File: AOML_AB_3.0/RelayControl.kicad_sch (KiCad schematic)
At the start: 41 parts, among them IC1 CD4043BDR, IC2 CD4043BDR, J5 Conn_01x03, K1 TX2-L2-5V, K10 TX2-L2-5V, K11 TX2-L2-5V, K12 TX2-L2-5V, K13 TX2-L2-5V, K2 TX2-L2-5V, K3 TX2-L2-5V, K4 TX2-L2-5V, K5 TX2-L2-5V, K6 TX2-L2-5V, K7 TX2-L2-5V, K8 TX2-L2-5V, K9 TX2-L2-5V, U10 TLP170AM, U11 TLP170AM, U12 TLP170AM, U13 TLP170AM, U14 TLP170AM, U5 ULN2003, U6 ULN2003, U7 TLP170AM, U8 TLP170AM, U9 TLP170AM

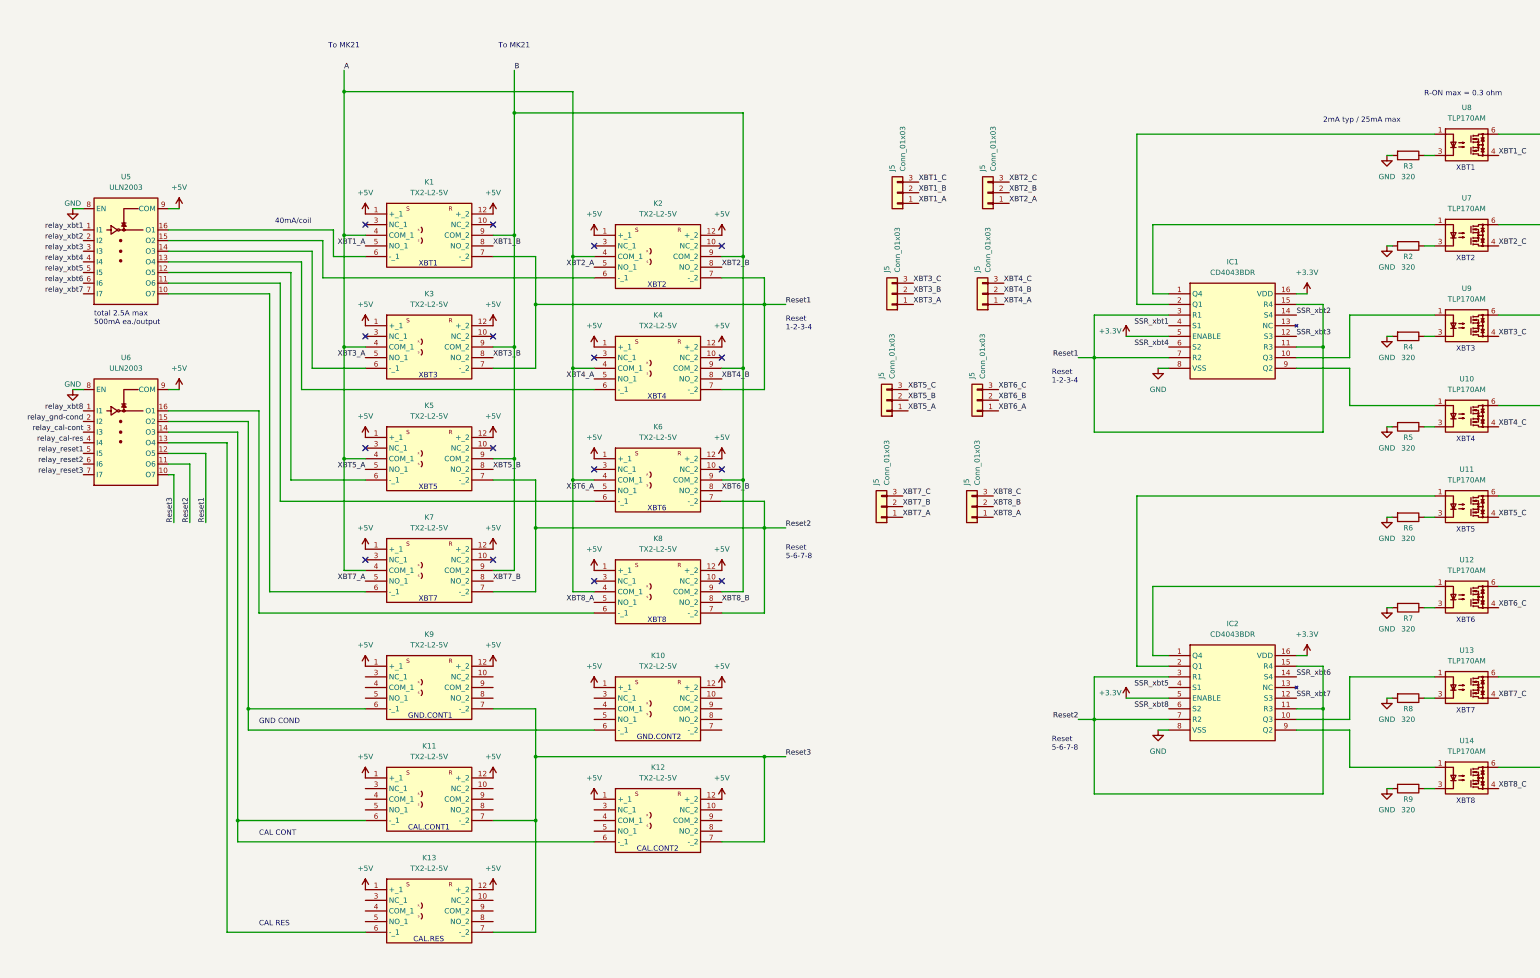
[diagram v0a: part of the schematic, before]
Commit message: footprints selected 99%, current sense added
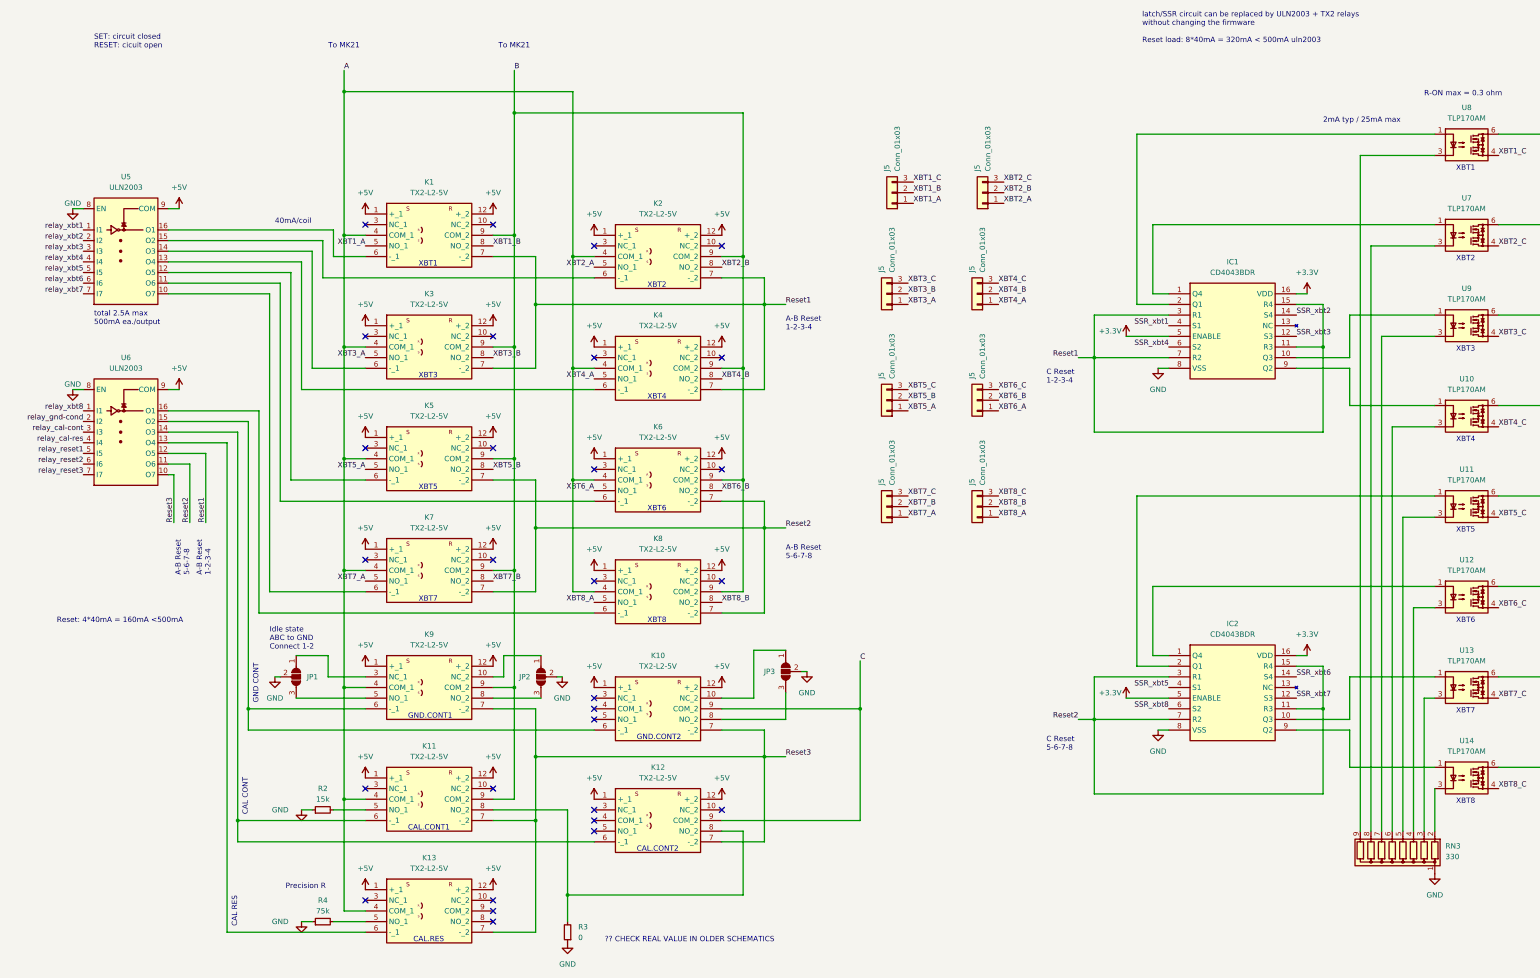
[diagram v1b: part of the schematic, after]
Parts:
- removed J5 (x7): Conn_01x03, symbol Connector_Generic:Conn_01x03
- removed R2, R3, R4, R5, R6, R7, R8, R9: 320, symbol Device:R
- added J5 (x7): Conn_01x03, Molex_3x1_0436500315:CON_436500315_MOL, symbol Connector_Generic:Conn_01x03
- added JP1, JP2, JP3: SolderJumper_3_Open, Jumper:SolderJumper-3_P1.3mm_Bridged12_Pad1.0x1.5mm, symbol Jumper:SolderJumper_3_Open
- added R2: 15k, symbol Device:R_Small
- added R3: 0, symbol Device:R_Small
- added R4: 75k, symbol Device:R_Small
- added RN3: 330, Resistor_THT:R_Array_SIP9, symbol Device:R_Network08
- J5: footprint (none) -> Molex_3x1_0436500315:CON_436500315_MOL; Digikey (none) -> https://www.digikey.com/en/products/detail/molex/0436500315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
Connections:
- net A: now also K11.4 (COM_1), K13.4 (COM_1), K9.4 (COM_1)
- net B: now also K11.9 (COM_2), K9.9 (COM_2)
- net C: now also K10.9 (COM_2), K12.9 (COM_2)
- net GND: now also JP1.2 (C), JP2.2 (C), JP3.2 (C), R2.1, R3.1, R4.1, RN3.1 (common)
- net Reset3: now also K10.7 (-_2)
- net XBT2_A: now also J5.1 (Pin_1)
- net XBT2_B: now also J5.2 (Pin_2)
- net XBT2_C: now also J5.3 (Pin_3)
- net XBT3_A: now also J5.1 (Pin_1)
- net XBT3_B: now also J5.2 (Pin_2)
- net XBT3_C: now also J5.3 (Pin_3)
- net XBT4_A: now also J5.1 (Pin_1)
- net XBT4_B: now also J5.2 (Pin_2)
- net XBT4_C: now also J5.3 (Pin_3)
- net XBT5_A: now also J5.1 (Pin_1)
- net XBT5_B: now also J5.2 (Pin_2)
- net XBT5_C: now also J5.3 (Pin_3)
- net XBT6_A: now also J5.1 (Pin_1)
- net XBT6_B: now also J5.2 (Pin_2)
- net XBT6_C: now also J5.3 (Pin_3)
- net XBT7_A: now also J5.1 (Pin_1)
- net XBT7_B: now also J5.2 (Pin_2)
- net XBT7_C: now also J5.3 (Pin_3)
- net XBT8_A: now also J5.1 (Pin_1)
- net XBT8_B: now also J5.2 (Pin_2)
- net XBT8_C: now also J5.3 (Pin_3)
- net at U11.3: now also RN3.5 (R4)
- net at U9.3: now also RN3.7 (R6)
- net at U13.3: now also RN3.3 (R2)
- net at K11.5 (NO_1): now also R2.2
- net at K11.8 (NO_2): now also K12.8 (NO_2), R3.2
- net at U10.3: now also RN3.6 (R5)
- net at K9.10 (NC_2): now also JP2.1 (A)
- net at K9.3 (NC_1): now also JP1.1 (A)
- net at K9.5 (NO_1): now also JP1.3 (B)
- net at K9.8 (NO_2): now also JP2.3 (B)
- net at U12.3: now also RN3.4 (R3)
- net at U8.3: now also RN3.9 (R8)
- net at U14.3: now also RN3.2 (R1)
- net at U7.3: now also RN3.8 (R7)
- net at K10.10 (NC_2): now also JP3.1 (A)
- net at K10.8 (NO_2): now also JP3.3 (B)
- net at K13.5 (NO_1): now also R4.2
- no-connect marks 16 -> 29
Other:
- note added: "?? CHECK REAL VALUE IN OLDER SCHEMATICS"
- note added: "A-B Reset 1-2-3-4"
- note added: "A-B Reset 5-6-7-8"
- note added: "C Reset 1-2-3-4"
- note added: "C Reset 5-6-7-8"
- note added: "GND CONT"
- note added: "Idle state ABC to GND Connect 1-2"
- note added: "Precision R"
- note added: "Reset: 4*40mA = 160mA <500mA"
- note added: "SET: circuit closed RESET: cicuit open"
- note added: "latch/SSR circuit can be replaced by ULN2003 + TX2 relays without changing the firmware Reset load: 8*40mA = 320mA < 500mA uln2003"
- note removed: "GND COND"
- note removed: "Reset 1-2-3-4"
- note removed: "Reset 5-6-7-8"
- company: (none) -> NOAA/AOML
- title: (none) -> XBT Autolauncher 3.0
- moved on the sheet: J5

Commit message: schematic finished, 100% footprints selected, check rules OK, Diego's V2.3 found (V2.3 CAL & COND relays w/5k and 15k resistor connections were used in V3.0)
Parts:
- removed K12: TX2-L2-5V, TX2L25V, symbol Relay_TX-L2-5V_2:TX2-L2-5V
- removed R4: 75k, symbol Device:R_Small
- R2: value 15k -> 5k; footprint (none) -> Precision_resistor_5k:Y1453_VIS; Digikey (none) -> https://www.digikey.com/en/products/detail/vpg-foil-resisto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
- R3: value 0 -> 15k; footprint (none) -> Resistor_THT:R_Axial_DIN0207_L6.3mm_D2.5mm_P7.62mm_Horizontal; Digikey (none) -> https://www.digikey.com/en/products/detail/yageo/CFR-25JR-5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
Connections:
- net GND: no longer R2.1
- net at K11.5 (NO_1): now also K11.8 (NO_2), R2.1, R3.2; no longer R2.2
- net at K13.5 (NO_1): now also R2.2
- net A renamed xbt_A
- net xbt_A: no longer K11.4 (COM_1)
- net B renamed xbt_B
- net C renamed xbt_C
- net xbt_C: now also K11.4 (COM_1)
- net relay_cal-cont renamed relay_cal_cont
- net relay_cal-res renamed relay_cal_res
- net relay_gnd-cond renamed relay_gnd_cond
- no-connect marks 29 -> 25
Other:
- note added: "Regular 5% R"
- note added: "Removed 1 relay from V2.3 RLY3 & RLY4 were combined in 1 relay"
- note removed: "?? CHECK REAL VALUE IN OLDER SCHEMATICS"
- note removed: "CAL.CONT2"

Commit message: PCB errors corrected, pad numbers corrected, PCB organization started
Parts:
- removed U6: ULN2003, symbol ULN2003AN:ULN2003
- added U5: ULN2003ADR, Relay_driver_ULN2003ADR:D0016A_L, symbol ULN2003AN:ULN2003
- JP1, JP2, JP3: footprint Jumper:SolderJumper-3_P1.3mm_Bridged12_Pad1.0x1.5mm -> Jumper:SolderJumper-3_P1.3mm_Open_RoundedPad1.0x1.5mm
- K1, K10, K11, K13, K2, K3, K4, K5, K6, K7, K8, K9: footprint TX2L25V -> Relay_TX-L2-5V:RELAY_TX2_L2_PAN
- U5: value ULN2003 -> ULN2003ADR; footprint (none) -> Relay_driver_ULN2003ADR:D0016A_L; Digikey (none) -> https://www.digikey.com/en/products/detail/texas-instrument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
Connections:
- net +5V: now also U5.9 (COM)
- net GND: now also U5.8 (EN)
- net Reset1: now also U5.12 (O5)
- net Reset2: now also U5.11 (O6)
- net Reset3: now also U5.10 (O7)
- net relay_cal_cont: now also U5.3 (I3)
- net relay_cal_res: now also U5.4 (I4)
- net relay_gnd_cond: now also U5.2 (I2)
- net relay_reset1: now also U5.5 (I5)
- net relay_reset2: now also U5.6 (I6)
- net relay_reset3: now also U5.7 (I7)
- net relay_xbt8: now also U5.1 (I1)
- net at K11.6 (-_1): now also U5.14 (O3)
- net at K10.6 (-_1), K9.6 (-_1): now also U5.15 (O2)
- net at K13.6 (-_1): now also U5.13 (O4)
- net at K8.6 (-_1): now also U5.16 (O1)

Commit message: PBC edge and final footprint review, jlpcb restrictions revised
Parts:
- IC1, IC2: footprint SOIC127P600X175-16N -> Latch_CD4043BDR:SOIC127P600X175-16N
- RN3: footprint Resistor_THT:R_Array_SIP9 -> Resistor_network-330:RESCAV80P400X210X65-10N; Digikey https://www.digikey.com/en/products/detail/yageo/YC158TJR-0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 -> https://www.digikey.com/en/products/detail/panasonic-electr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
- renumbered JP1 to JP6, JP2 to JP7, JP3 to JP8, R2 to R10, R3 to R11, U8 to U10, U7 to U11, U9 to U12, U10 to U13, U11 to U14, U12 to U15, U13 to U16, U14 to U17
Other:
- moved on the sheet: J5
